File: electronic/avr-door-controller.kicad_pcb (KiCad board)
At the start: 2 copper layers, 110 x 56 mm, 73 parts, among them CON1 24V, J1 DOOR1, J2 DOOR2, P1 Digital, P10 DOOR2 BTN, P2 Analog, P3 DOOR1 BTN, P4 RELAY1, P5 RELAY1 CTRL, P6 USB_A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

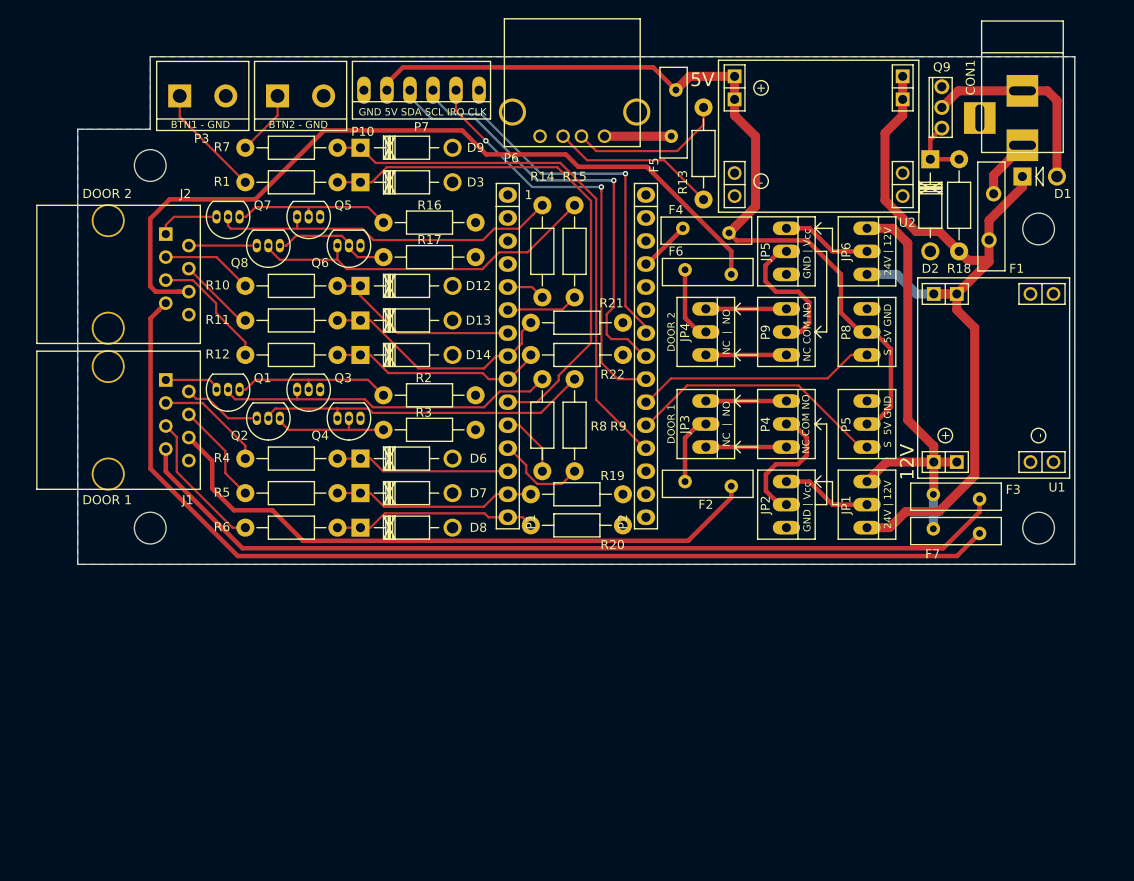
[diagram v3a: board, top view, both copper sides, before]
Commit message: electronic: pcb: Completely rework the PCB for rev 2
This is a completely new PCB with integrated relays, 24V step-up and
enought space for the RTC module. It has been design to fit in an RND
455-00119 case.

Signed-off-by: Alban Bedel <alban.bedel@avionic-design.de>
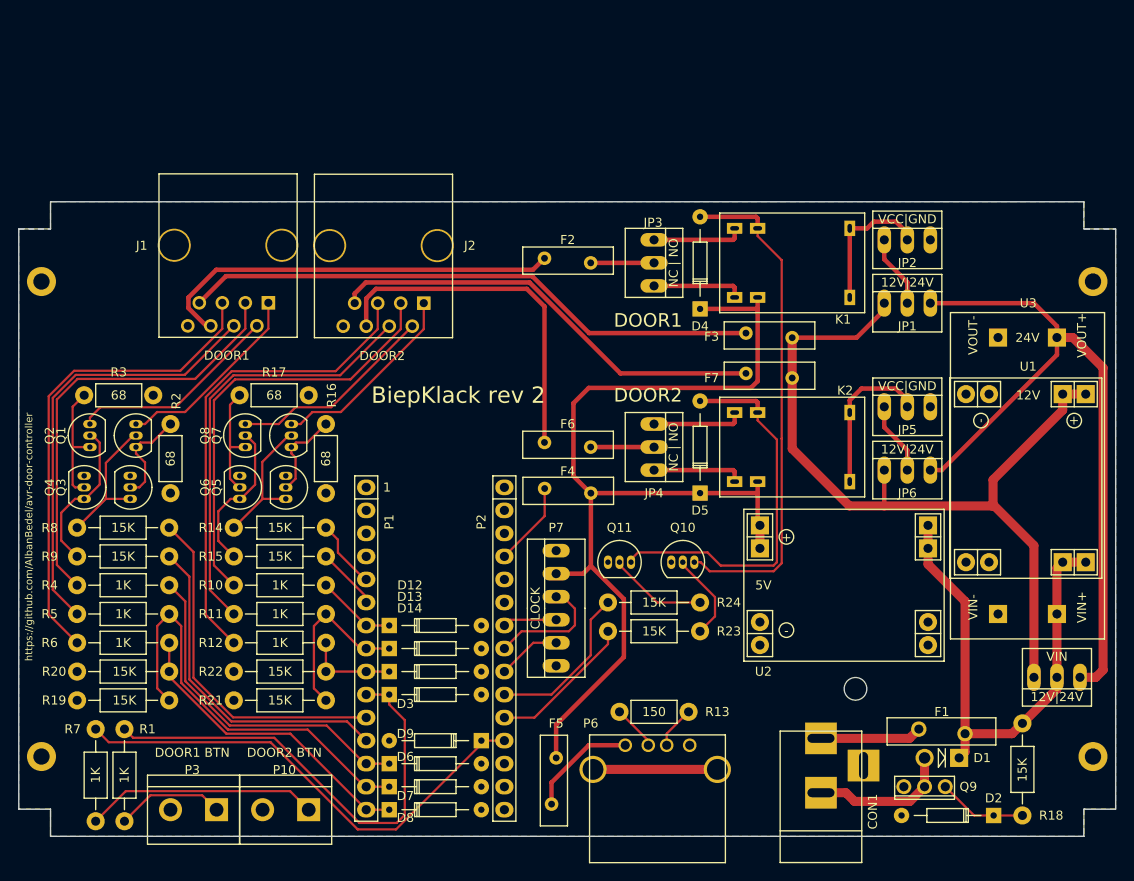
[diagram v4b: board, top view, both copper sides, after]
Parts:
- removed P4: RELAY1, Connect:PINHEAD1-3
- removed P5: RELAY1 CTRL, Connect:PINHEAD1-3
- removed P8: RELAY2 CTRL, Connect:PINHEAD1-3
- removed P9: RELAY2, Connect:PINHEAD1-3
- removed the REF** at (198.0, 75.0)
- removed the REF** at (198.0, 108.0)
- removed the REF** at (100.0, 68.0)
- removed the REF** at (100.0, 108.0)
- added D4: 1N4148, Diodes_ThroughHole:Diode_DO-35_SOD27_Horizontal_RM10, F.Cu at (160.7, 83.8)
- added D5: 1N4148, Diodes_ThroughHole:Diode_DO-35_SOD27_Horizontal_RM10, F.Cu at (160.7, 104.1)
- added JP7: 12V|24V, Connect:PINHEAD1-3, F.Cu at (200.0, 124.5)
- added K1: RELAY, Modules:JRC-21F, F.Cu at (170.8, 78.7)
- added K2: RELAY, Modules:JRC-21F, F.Cu at (170.8, 99.1)
- added Q10: Q_NPN_EBC, TO_SOT_Packages_THT:TO-92_Inline_Narrow_Oval, F.Cu at (157.5, 111.8)
- added Q11: Q_NPN_EBC, TO_SOT_Packages_THT:TO-92_Inline_Narrow_Oval, F.Cu at (150.5, 111.8)
- added R23: 15K, Resistors_ThroughHole:Resistor_Horizontal_RM10mm, F.Cu at (160.7, 119.4)
- added R24: 15K, Resistors_ThroughHole:Resistor_Horizontal_RM10mm, F.Cu at (160.7, 116.2)
- added REF**: MountingHole_2-5mm, Mounting_Holes:MountingHole_2-5mm, F.Cu at (204.0, 133.2)
- added REF**: MountingHole_2-5mm, Mounting_Holes:MountingHole_2-5mm, F.Cu at (88.0, 133.2)
- added REF**: MountingHole_2-5mm, Mounting_Holes:MountingHole_2-5mm, F.Cu at (88.0, 80.8)
- added REF**: MountingHole_2-5mm, Mounting_Holes:MountingHole_2-5mm, F.Cu at (204.0, 80.8)
- added REF**: MountingHole_2-5mm, Mounting_Holes:MountingHole_2-5mm, F.Cu at (177.8, 125.7)
- added U3: 24V, Modules:MT3608, F.Cu at (196.8, 102.2)
- D12, D13, D14, D2, D3, D6, D7, D8, D9: footprint Diodes_ThroughHole:Diode_DO-41_SOD81_Horizontal_RM10 -> Diodes_ThroughHole:Diode_DO-35_SOD27_Horizontal_RM10
- F4: value 0.17A -> 0.09A
- JP1: value DR1 VCC -> 12V|24V
- JP2: value DR1 LVL -> VCC|GND
- JP3: value DR1 NO/NC -> NC | NO
- JP4: value DR2 NO/NC -> NC | NO
- JP5: value DR2 LVL -> VCC|GND
- JP6: value DR2 VCC -> 12V|24V
- R13, R16, R17, R2, R3: footprint Resistors_ThroughHole:Resistor_Horizontal_RM10mm -> Resistors_ThroughHole:Resistor_Horizontal_RM7mm
- moved CON1 80.9 mm to (174.0, 137.4), turned to 90 degrees
- moved P10 78.8 mm to (114.9, 139.1), turned to 180 degrees
- moved P3 78.7 mm to (104.8, 139.1), turned to 180 degrees
- moved R7 76.1 mm to (94.0, 140.3), turned to 90 degrees
- moved F5 74.9 mm to (144.8, 133.3)
- moved R18 72.7 mm to (196.2, 139.7), turned to 90 degrees
- moved D2 72.7 mm to (193.0, 139.7), turned to 180 degrees
- moved Q9 72.6 mm to (187.7, 136.5), turned to 180 degrees
- moved R1 71.7 mm to (97.2, 140.3), turned to 90 degrees
- moved P6 67.2 mm to (152.4, 132.0), turned to 0 degrees
- moved D9 66.7 mm to (136.5, 131.4), turned to 180 degrees
- moved D1 64.5 mm to (189.2, 133.3), turned to 180 degrees
- moved R20 62.3 mm to (91.9, 123.8), turned to 0 degrees
- moved R21 59.8 mm to (109.2, 127.0), turned to 0 degrees
- moved F1 59.6 mm to (184.8, 130.2), turned to 0 degrees
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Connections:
- D1 pad 1: +24V -> Net-(D1-Pad1)
- F1 pad 2: +24V -> Net-(D1-Pad1)
- JP2 pad 2: /RELAY1_COM -> Net-(JP2-Pad2)
- JP3 pad 1: /RELAY1_NO -> Net-(JP3-Pad1)
- JP3 pad 3: /RELAY1_NC -> Net-(JP3-Pad3)
- JP4 pad 1: /RELAY2_NO -> Net-(JP4-Pad1)
- JP4 pad 3: /RELAY2_NC -> Net-(JP4-Pad3)
- JP5 pad 2: /RELAY2_COM -> Net-(JP5-Pad2)
- R18 pad 2: +24V -> Net-(D1-Pad1)
- U1 pad 1: +24V -> Net-(D1-Pad1)
- U1 pad 2: +24V -> Net-(D1-Pad1)
- U2 pad 1: +24V -> Net-(D1-Pad1)
- U2 pad 2: +24V -> Net-(D1-Pad1)
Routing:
- net /DOOR2_12V: track 115.4 -> 48.9 mm
- net Net-(D1-Pad1): track 0.00 -> 57.3 mm
- net Net-(D4-Pad2): track 0.00 -> 56.0 mm
- net /DOOR2_RELAY: track 88.1 -> 39.0 mm
- net +12V: track 48.7 -> 92.1 mm
- net Net-(D5-Pad2): track 0.00 -> 42.4 mm
- net /A3: track 46.9 -> 7.03 mm, vias 2 -> 0
- net /DOOR2_D0: track 13.6 -> 53.3 mm
- net /DOOR2_D1: track 8.60 -> 47.9 mm
- net /A5: track 44.0 -> 5.98 mm, vias 1 -> 0
- net /DOOR2_STATUS: track 10.1 -> 48.0 mm
- net /DOOR1_D0: track 15.7 -> 53.6 mm
- net /DOOR1_D1: track 11.3 -> 48.2 mm
- net /A4: track 49.7 -> 13.3 mm, vias 1 -> 0
- net /DOOR1_STATUS: track 12.1 -> 48.3 mm
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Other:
- board size 110 x 56 mm -> 121 x 70 mm
- net class Default: via_drill 0.3 -> 0.4
- rule trace_min: 0.1 -> 0.2
- rule via_min_drill: 0.2 -> 0.3
- rule via_min_size: 0.45 -> 0.4
- board text added: "BiepKlack rev 2"
- board text added: "DOOR1"
- board text added: "DOOR2"
- board text added: "RND 455-00119"
- board text added: "VIN"
- board text added: "https://github.com/AlbanBedel/avr-door-controller"
- board text removed: "12V"
- board text removed: "24V | 12V"
- board text removed: "5V"
- board text removed: "BTN1 - GND"
- board text removed: "BTN2 - GND"
- board text removed: "DOOR 1"
- board text removed: "DOOR 2"
- board text removed: "GND 5V SDA SCL IRQ CLK"
- board text removed: "GND | Vcc"
- board text removed: "NC COM NO"
- board text removed: "NC | NO"
- board text removed: "S 5V GND"

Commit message: electronic: pcb: Increase the mounting holes size to 3mm
The screw holes in the hounsing are a bit larger than expected. To
properly attach the PCB we need 3mm holes instead of 2.5mm.

Signed-off-by: Alban Bedel <albeu@free.fr>
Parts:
- REF** (x4): footprint Mounting_Holes:MountingHole_2-5mm -> Mounting_Holes:MountingHole_3mm
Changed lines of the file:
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@@
     (links 157)
     (no_connects 0)
-    (area 85.424999 71.924999 206.575001 142.075001)
+    (area 58.500001 37.15 240.5 148.52)
     (thickness 1.6)
     (drawings 46)
@@
     )
   )
-  (module Mounting_Holes:MountingHole_2-5mm (layer F.Cu)
-    (at 204 133.2)
-    (descr "Mounting hole, Befestigungsbohrung, 2,5mm, No Annular, Kein Restring,")
-    (tags "Mounting hole, Befestigungsbohrung, 2,5mm, No Annular, Kein Restring,")
-    (fp_text reference REF** (at 0 -3.50012) (layer F.SilkS) hide
-      (effects (font (size 1 1) (thickness 0.15)))
-    )
-    (fp_text value MountingHole_2-5mm (at 0.09906 3.59918) (layer F.Fab) hide
-      (effects (font (size 1 1) (thickness 0.15)))
-    )
-    (fp_circle (center 0 0) (end 2.5 0) (layer Cmts.User) (width 0.381))
-    (pad "" np_thru_hole circle (at 0 0) (size 3.2 3.2) (drill 1.8) (layers *.Cu *.Mask F.SilkS))
-  )
-  (module Mounting_Holes:MountingHole_2-5mm (layer F.Cu)
-    (at 88 133.2)
-    (descr "Mounting hole, Befestigungsbohrung, 2,5mm, No Annular, Kein Restring,")
-    (tags "Mounting hole, Befestigungsbohrung, 2,5mm, No Annular, Kein Restring,")
-    (fp_text reference REF** (at 0 -3.50012) (layer F.SilkS) hide
-      (effects (font (size 1 1) (thickness 0.15)))
-    )
-    (fp_text value MountingHole_2-5mm (at 0.09906 3.59918) (layer F.Fab) hide
-      (effects (font (size 1 1) (thickness 0.15)))
-    )
-    (fp_circle (center 0 0) (end 2.5 0) (layer Cmts.User) (width 0.381))
-    (pad "" np_thru_hole circle (at 0 0) (size 3.2 3.2) (drill 1.8) (layers *.Cu *.Mask F.SilkS))
-  )
-  (module Mounting_Holes:MountingHole_2-5mm (layer F.Cu)
-    (at 88 80.8)
-    (descr "Mounting hole, Befestigungsbohrung, 2,5mm, No Annular, Kein Restring,")
-    (tags "Mounting hole, Befestigungsbohrung, 2,5mm, No Annular, Kein Restring,")
-    (fp_text reference REF** (at 0 -3.50012) (layer F.SilkS) hide
-      (effects (font (size 1 1) (thickness 0.15)))
-    )
-    (fp_text value MountingHole_2-5mm (at 0.09906 3.59918) (layer F.Fab)
-      (effects (font (size 1 1) (thickness 0.15)))
-    )
-    (fp_circle (center 0 0) (end 2.5 0) (layer Cmts.User) (width 0.381))
-    (pad "" np_thru_hole circle (at 0 0) (size 3.2 3.2) (drill 1.8) (layers *.Cu *.Mask F.SilkS))
-  )
   (module Connect:RJ45_8 (layer F.Cu)
     (at 108.585 76.795 180)
@@
     )
   )
-  (module Mounting_Holes:MountingHole_2-5mm (layer F.Cu)
-    (at 204 80.8)
-    (descr "Mounting hole, Befestigungsbohrung, 2,5mm, No Annular, Kein Restring,")
-    (tags "Mounting hole, Befestigungsbohrung, 2,5mm, No Annular, Kein Restring,")
-    (fp_text reference REF** (at 0 -3.50012) (layer F.SilkS) hide
-      (effects (font (size 1 1) (thickness 0.15)))
-    )
-    (fp_text value MountingHole_2-5mm (at 0.09906 3.59918) (layer F.Fab) hide
-      (effects (font (size 1 1) (thickness 0.15)))
-    )
-    (fp_circle (center 0 0) (end 2.5 0) (layer Cmts.User) (width 0.381))
-    (pad "" np_thru_hole circle (at 0 0) (size 3.2 3.2) (drill 1.8) (layers *.Cu *.Mask F.SilkS))
-  )
   (module Connect:PINHEAD1-3 (layer F.Cu)
     (at 155.575 99.06 270)
@@
       (net 47 +24V))
   )
+  (module Mounting_Holes:MountingHole_3mm (layer F.Cu)
+    (at 88 80.8)
+    (descr "Mounting hole, Befestigungsbohrung, 3mm, No Annular, Kein Restring,")
+    (tags "Mounting hole, Befestigungsbohrung, 3mm, No Annular, Kein Restring,")
+    (fp_text reference REF** (at 0 -4.0005) (layer F.SilkS) hide
+      (effects (font (size 1 1) (thickness 0.15)))
+    )
+    (fp_text value MountingHole_2-5mm (at 1.00076 5.00126) (layer F.Fab)
+      (effects (font (size 1 1) (thickness 0.15)))
+    )
+    (fp_circle (center 0 0) (end 3 0) (layer Cmts.User) (width 0.381))
+    (pad 1 thru_hole circle (at 0 0) (size 3 3) (drill 3) (layers))
+  )
+  (module Mounting_Holes:MountingHole_3mm (layer F.Cu)
+    (at 88 133.2)
+    (descr "Mounting hole, Befestigungsbohrung, 3mm, No Annular, Kein Restring,")
+    (tags "Mounting hole, Befestigungsbohrung, 3mm, No Annular, Kein Restring,")
+    (fp_text reference REF** (at 0 -4.0005) (layer F.SilkS) hide
+      (effects (font (size 1 1) (thickness 0.15)))
+    )
+    (fp_text value MountingHole_2-5mm (at 1.00076 5.00126) (layer F.Fab)
+      (effects (font (size 1 1) (thickness 0.15)))
+    )
+    (fp_circle (center 0 0) (end 3 0) (layer Cmts.User) (width 0.381))
+    (pad 1 thru_hole circle (at 0 0) (size 3 3) (drill 3) (layers))
+  )
+  (module Mounting_Holes:MountingHole_3mm (layer F.Cu)
+    (at 204 133.2)
+    (descr "Mounting hole, Befestigungsbohrung, 3mm, No Annular, Kein Restring,")
+    (tags "Mounting hole, Befestigungsbohrung, 3mm, No Annular, Kein Restring,")
+    (fp_text reference REF** (at 0 -4.0005) (layer F.SilkS) hide
+      (effects (font (size 1 1) (thickness 0.15)))
+    )
+    (fp_text value MountingHole_2-5mm (at 1.00076 5.00126) (layer F.Fab)
+      (effects (font (size 1 1) (thickness 0.15)))
+    )
+    (fp_circle (center 0 0) (end 3 0) (layer Cmts.User) (width 0.381))
+    (pad 1 thru_hole circle (at 0 0) (size 3 3) (drill 3) (layers))
+  )
+  (module Mounting_Holes:MountingHole_3mm (layer F.Cu)
+    (at 204 80.8)
+    (descr "Mounting hole, Befestigungsbohrung, 3mm, No Annular, Kein Restring,")
+    (tags "Mounting hole, Befestigungsbohrung, 3mm, No Annular, Kein Restring,")
+    (fp_text reference REF** (at 0 -4.0005) (layer F.SilkS) hide
+      (effects (font (size 1 1) (thickness 0.15)))
+    )
+    (fp_text value MountingHole_2-5mm (at 1.00076 5.00126) (layer F.Fab)
+      (effects (font (size 1 1) (thickness 0.15)))
+    )
+    (fp_circle (center 0 0) (end 3 0) (layer Cmts.User) (width 0.381))
+    (pad 1 thru_hole circle (at 0 0) (size 3 3) (drill 3) (layers))
+  )
   (gr_text https://github.com/AlbanBedel/avr-door-controller (at 86.614 108.966 90) (layer F.SilkS)
